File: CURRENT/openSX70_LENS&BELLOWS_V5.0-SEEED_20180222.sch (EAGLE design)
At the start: 45 parts, among them Q1 5.8A/30V/35mΩ, Q2 5.8A/30V/35mΩ, U1 ATMEGA328P_TQFP, U3 BH1750FVI-TR, Y1 CSTCE8M00G52Z-R0

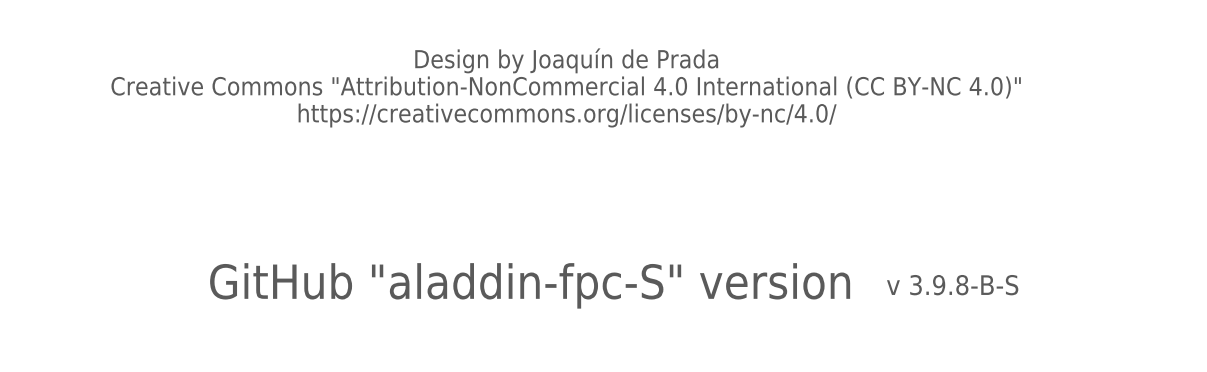
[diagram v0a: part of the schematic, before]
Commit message: New board nickname: Len's&Bellows 5.0 (different from Len's & Bellows 4.x): moved Atmega up, and much more little improvements!
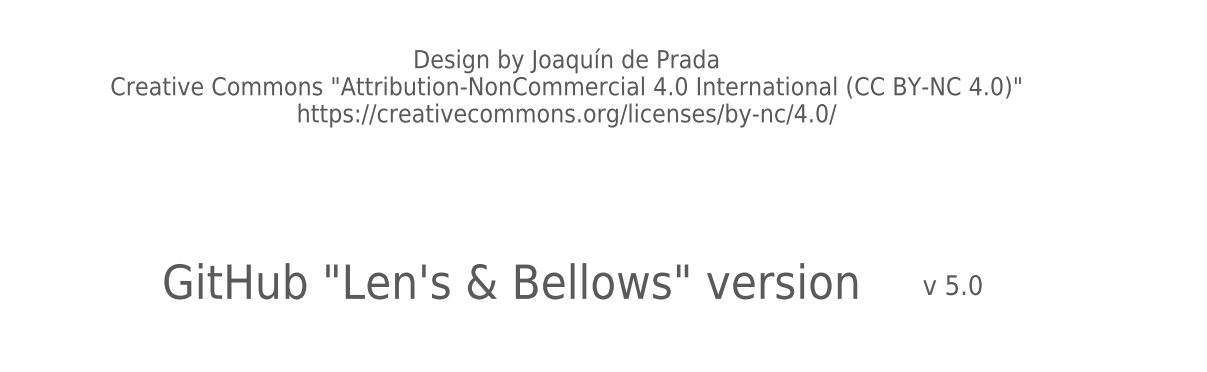
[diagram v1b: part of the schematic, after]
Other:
- note added: "GitHub "Len's & Bellows" version"
- note added: "v 5.0"
- note removed: "GitHub "aladdin-fpc-S" version"
- note removed: "v 3.9.8-B-S"
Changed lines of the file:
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@@
 or
 FLASH</text>
-<text x="246.38" y="2.54" size="2.1844" layer="97" align="center">v 3.9.8-B-S</text>
+<text x="246.38" y="2.54" size="2.1844" layer="97" align="center">v 5.0</text>
 <text x="203.454" y="24.638" size="2.0066" layer="97" align="center">Design by Joaquín de Prada
 Creative Commons "Attribution-NonCommercial 4.0 International (CC BY-NC 4.0)"
 https://creativecommons.org/licenses/by-nc/4.0/</text>
-<text x="163.576" y="1.016" size="3.81" layer="97">GitHub "aladdin-fpc-S" version</text>
+<text x="158.496" y="1.016" size="3.81" layer="97">GitHub "Len's &amp; Bellows" version</text>
 <text x="139.7" y="38.1" size="1.6764" layer="97">DEFAULT 6V
 ONLY 6V OR 3.3V

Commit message: All ready for manufacture!
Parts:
- R15: value 100R -> 0R
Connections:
- new net 0R: U$4.3
- net 100R: no longer U$4.3
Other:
- note added: "MISO"
- note added: "MOSI"
- note added: "RESET"
- note added: "SCK"
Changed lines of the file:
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@@
 <part name="D3" library="Common-Parts-Library-Eagle" deviceset="1N4148WS" device="" value="1N4148WSF"/>
 <part name="U$4" library="Seeed-OPL-2017-01-connector-edward" deviceset="SMD-FPC-CONN-0512810594" device="&quot;"/>
-<part name="R15" library="Seeed-Resistor" library_urn="urn:adsk.eagle:library:474" deviceset="SMD-RES-100R-5%-1/10W(0603)" device="" package3d_urn="urn:adsk.eagle:package:32791/1" value="100R"/>
+<part name="R15" library="Seeed-Resistor" library_urn="urn:adsk.eagle:library:474" deviceset="SMD-RES-100R-5%-1/10W(0603)" device="" package3d_urn="urn:adsk.eagle:package:32791/1" value="0R"/>
 <part name="JP2" library="SparkFun-Jumpers" deviceset="JUMPER-SMT_3_1-NC_TRACE" device="_SILK" value="FTDI VCC SELECTOR"/>
 <part name="P+9" library="openSX70" deviceset="VCC" device="" value="6V"/>
@@
 </text>
 <text x="58.42" y="167.64" size="5.08" layer="95" font="vector">SEEEDSTUDIO FUSION VERSION ONLY 5P-FPC</text>
+<text x="55.88" y="43.18" size="1.778" layer="96">MISO</text>
+<text x="55.88" y="40.64" size="1.778" layer="96">SCK</text>
+<text x="55.88" y="38.1" size="1.778" layer="96">RESET</text>
+<text x="96.52" y="40.64" size="1.778" layer="96">MOSI</text>
 </plain>
 <instances>
@@
 <instance part="R9" gate="G$1" x="12.7" y="63.5" smashed="yes">
 <attribute name="NAME" x="10.922" y="65.2526" size="1.778" layer="95"/>
-<attribute name="VALUE" x="10.668" y="59.69" size="1.778" layer="96"/>
+<attribute name="VALUE" x="8.128" y="59.69" size="1.778" layer="96"/>
 </instance>
 <instance part="R10" gate="G$1" x="27.94" y="63.5" smashed="yes">
@@
 <instance part="GND12" gate="1" x="238.76" y="137.16"/>
 <instance part="P+5" gate="VCC" x="167.64" y="147.32" rot="R90"/>
-<instance part="GND16" gate="1" x="27.94" y="0"/>
+<instance part="GND16" gate="1" x="27.94" y="2.54"/>
 <instance part="C2" gate="G$1" x="93.98" y="9.144" smashed="yes" rot="R270">
 <attribute name="NAME" x="91.186" y="11.43" size="1.27" layer="95" font="vector" ratio="10"/>
@@
 <wire x1="193.04" y1="104.14" x2="200.66" y2="104.14" width="0.1524" layer="91"/>
 <label x="195.58" y="104.14" size="1.778" layer="95"/>
-</segment>
-<segment>
-<label x="121.92" y="40.64" size="1.778" layer="95"/>
-<pinref part="U$4" gate="G$1" pin="3"/>
-<wire x1="127" y1="20.32" x2="127" y2="40.64" width="0.1524" layer="91"/>
-<label x="-10.16" y="22.86" size="1.778" layer="95"/>
 </segment>
 </net>
@@
 <pinref part="R8" gate="G$1" pin="1"/>
 <pinref part="GND16" gate="1" pin="GND"/>
-<wire x1="27.94" y1="2.54" x2="27.94" y2="3.81" width="0.1524" layer="91"/>
+<wire x1="27.94" y1="5.08" x2="27.94" y2="3.81" width="0.1524" layer="91"/>
 </segment>
 <segment>
@@
 </segment>
 </net>
+<net name="0R" class="0">
+<segment>
+<label x="121.92" y="40.64" size="1.778" layer="95"/>
+<pinref part="U$4" gate="G$1" pin="3"/>
+<wire x1="127" y1="20.32" x2="127" y2="40.64" width="0.1524" layer="91"/>
+<label x="-7.62" y="22.86" size="1.778" layer="95"/>
+</segment>
+</net>
